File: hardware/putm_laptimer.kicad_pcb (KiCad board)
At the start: 4 copper layers, 92 x 63.5 mm, 48 parts, among them J1 Conn_01x22, J10 Conn_01x07, J11 Conn_01x07, J12 Conn_01x05, J13 Conn_01x05, J14 2091-1376, J2 Conn_01x22, J3 Conn_01x22, J4 Conn_01x22, J7 Conn_02x05_Odd_Even, J8 Conn_01x09, J9 M80-5001805

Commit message: Fixed borders
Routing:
- net +3V3: track 38.7 -> 35.7 mm, vias 10 -> 9
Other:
- outline, holes or cut-outs redrawn
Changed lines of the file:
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@@
 	(layers
 		(0 "F.Cu" signal "SIG1")
-		(4 "In1.Cu" power "GND1")
-		(6 "In2.Cu" power "GND2")
+		(4 "In1.Cu" power "GND")
+		(6 "In2.Cu" power "POWER")
 		(2 "B.Cu" signal "SIG2")
 		(13 "F.Paste" user)
@@
 	)
 	(gr_line
-		(start 195.5 58.5)
-		(end 144.5 58.5)
+		(start 195.1 58.5)
+		(end 144.9 58.5)
 		(stroke
 			(width 0.1)
@@
 	(gr_line
 		(start 204 52.5)
-		(end 195.5 52.5)
+		(end 195.9 52.5)
+		(stroke
+			(width 0.1)
+			(type default)
+		)
+		(layer "Edge.Cuts")
+	)
+	(gr_line
+		(start 144.5 58.1)
+		(end 144.5 52.9)
+		(stroke
+			(width 0.1)
+			(type default)
+		)
+		(layer "Edge.Cuts")
+	)
+	(gr_arc
+		(start 195.5 58.1)
+		(mid 195.382843 58.382843)
+		(end 195.1 58.5)
 		(stroke
 			(width 0.1)
@@
 	)
 	(gr_arc
+		(start 195.5 52.9)
+		(mid 195.617157 52.617157)
+		(end 195.9 52.5)
+		(stroke
+			(width 0.1)
+			(type default)
+		)
+		(layer "Edge.Cuts")
+	)
+	(gr_arc
 		(start 116.5 57)
 		(mid 117.818019 53.818019)
@@
 	)
 	(gr_line
-		(start 195.5 58.5)
-		(end 195.5 52.5)
+		(start 195.5 58.1)
+		(end 195.5 52.9)
+		(stroke
+			(width 0.1)
+			(type default)
+		)
+		(layer "Edge.Cuts")
+	)
+	(gr_arc
+		(start 144.1 52.5)
+		(mid 144.382843 52.617157)
+		(end 144.5 52.9)
 		(stroke
 			(width 0.1)
@@
 	)
 	(gr_arc
-		(start 208.5 111.5)
-		(mid 207.181981 114.681981)
-		(end 204 116)
+		(start 144.9 58.5)
+		(mid 144.617157 58.382843)
+		(end 144.5 58.1)
 		(stroke
 			(width 0.1)
@@
 		(layer "Edge.Cuts")
 	)
-	(gr_line
-		(start 121 52.5)
-		(end 144.5 52.5)
+	(gr_arc
+		(start 208.5 111.5)
+		(mid 207.181981 114.681981)
+		(end 204 116)
 		(stroke
 			(width 0.1)
@@
 	)
 	(gr_line
-		(start 144.5 52.5)
-		(end 144.5 58.5)
+		(start 121 52.5)
+		(end 144.1 52.5)
 		(stroke
 			(width 0.1)
@@
 	)
 	(gr_text "LCD"
-		(at 145.39 93.5 0)
+		(at 145.5 96 0)
 		(layer "F.SilkS")
 		(effects
@@
 	)
 	(segment
-		(start 197.6 83.17)
-		(end 195.83 83.17)
-		(width 0.4)
-		(layer "F.Cu")
-		(net 13)
-	)
-	(segment
 		(start 143.5 66.85)
 		(end 143.5 66)
@@
 	)
 	(segment
-		(start 195.83 83.17)
-		(end 195 84)
-		(width 0.4)
-		(layer "F.Cu")
-		(net 13)
-	)
-	(segment
 		(start 142 84.5)
 		(end 141.825 84.325)
@@
 		(net 13)
 	)
-	(via
-		(at 195 84)
-		(size 0.5)
-		(drill 0.3)
-		(layers "F.Cu" "B.Cu")
-		(net 13)
-	)

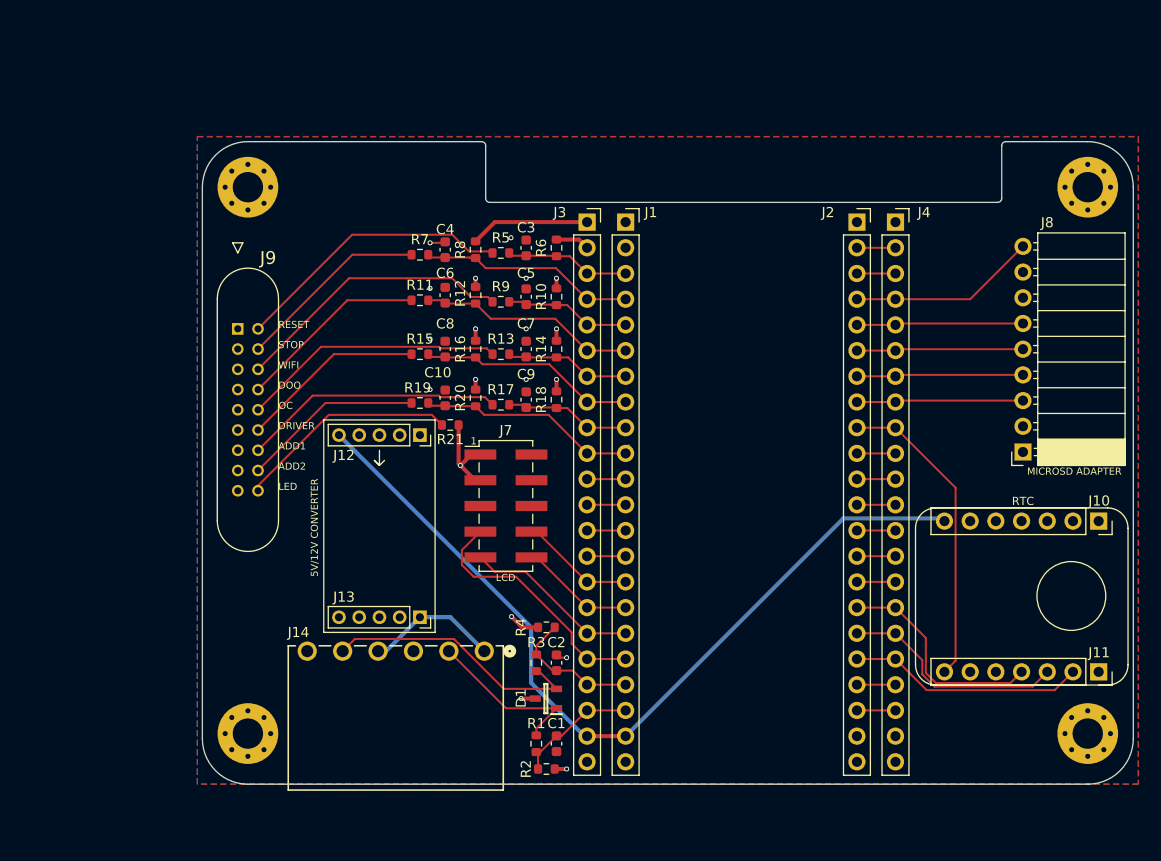
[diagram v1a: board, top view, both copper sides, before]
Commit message: Added modules info and links to connector schematics
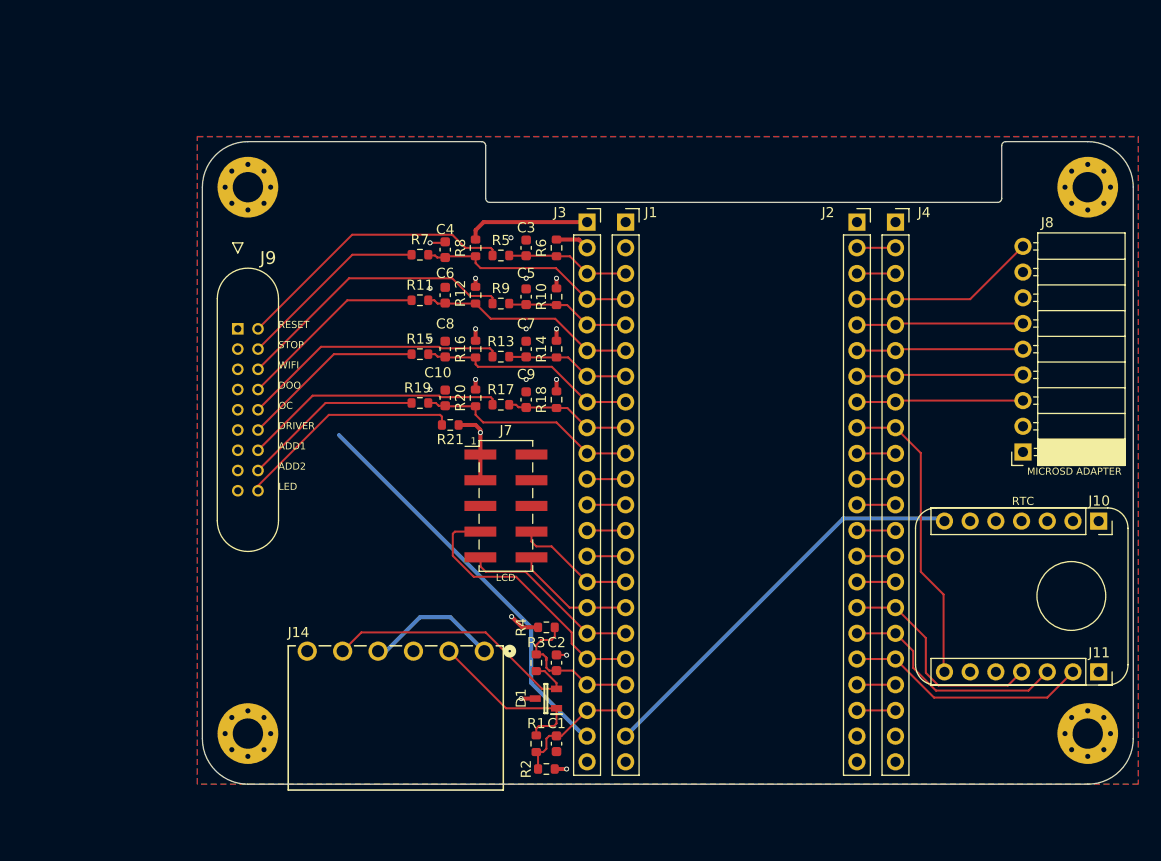
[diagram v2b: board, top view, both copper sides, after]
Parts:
- removed J12, J13: Conn_01x05, Connector_PinSocket_2.00mm:PinSocket_1x05_P2.00mm_Vertical
- moved R13 0.25 mm to (146.0, 73.8)
- moved R5 0.25 mm to (146.0, 63.8)
- moved R8 0.17 mm to (143.5, 63.0)
- moved R9 0.17 mm to (146.0, 68.5)
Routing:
- net +5V: track 84.8 -> 81.0 mm
- net /IO12_LCD_DC: track 24.7 -> 26.9 mm
- net /IO13_GATE2: track 13.7 -> 15.2 mm
- net /IO9_LCD_SPI_MOSI: track 11.4 -> 12.5 mm
- net +3V3: track 35.7 -> 34.6 mm
- net /IO39_RTC_NINT: track 30.9 -> 29.9 mm
- net Net-(D1-Pad2): track 26.9 -> 27.7 mm
- net Net-(D1-Pad1): track 16.5 -> 17.4 mm
- net /IO14_GATE1: track 13.5 -> 14.2 mm
- net /IO10_LCD_SPI_CS: track 11.4 -> 12.1 mm
- net /IO21_RTC_I2C_SCL: track 23.4 -> 24.0 mm
- net /IO11_LCD_SPI_CLK: track 17.9 -> 18.4 mm
- net /IO17_PIN: track 22.0 -> 22.5 mm
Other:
- board text removed: "5V/12V CONVERTER"

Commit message: Fixed routing
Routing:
- net +5V: track 81.0 -> 1.04 mm
- net +3V3: track 34.6 -> 61.7 mm, vias 9 -> 10
- net /ADD1_BTN: track 26.1 -> 28.7 mm, vias 0 -> 1
- net /OC_BTN: track 26.2 -> 28.3 mm, vias 0 -> 1
- net GND: track 3.95 -> 2.55 mm, vias 10 -> 5
- net /IO21_RTC_I2C_SCL: track 24.0 -> 25.3 mm
- net /PWR_LED: track 22.5 -> 21.4 mm, vias 0 -> 1
- net /IO47_RTC_I2C_SDA: track 22.9 -> 23.5 mm
- net /WIFI_BTN: track 28.1 -> 28.7 mm, vias 0 -> 1
- net /RST_BTN: track 28.0 -> 27.7 mm, vias 0 -> 1
- net /DOO_BTN: track 18.8 -> 19.0 mm, vias 0 -> 1
- net /STOP_BTN: vias 0 -> 1
- net /DRIVER_BTN: vias 0 -> 1
- net /ADD2_BTN: vias 0 -> 1
- added copper zone on In2.Cu, net +12V
- added copper zone on In2.Cu, net +5V

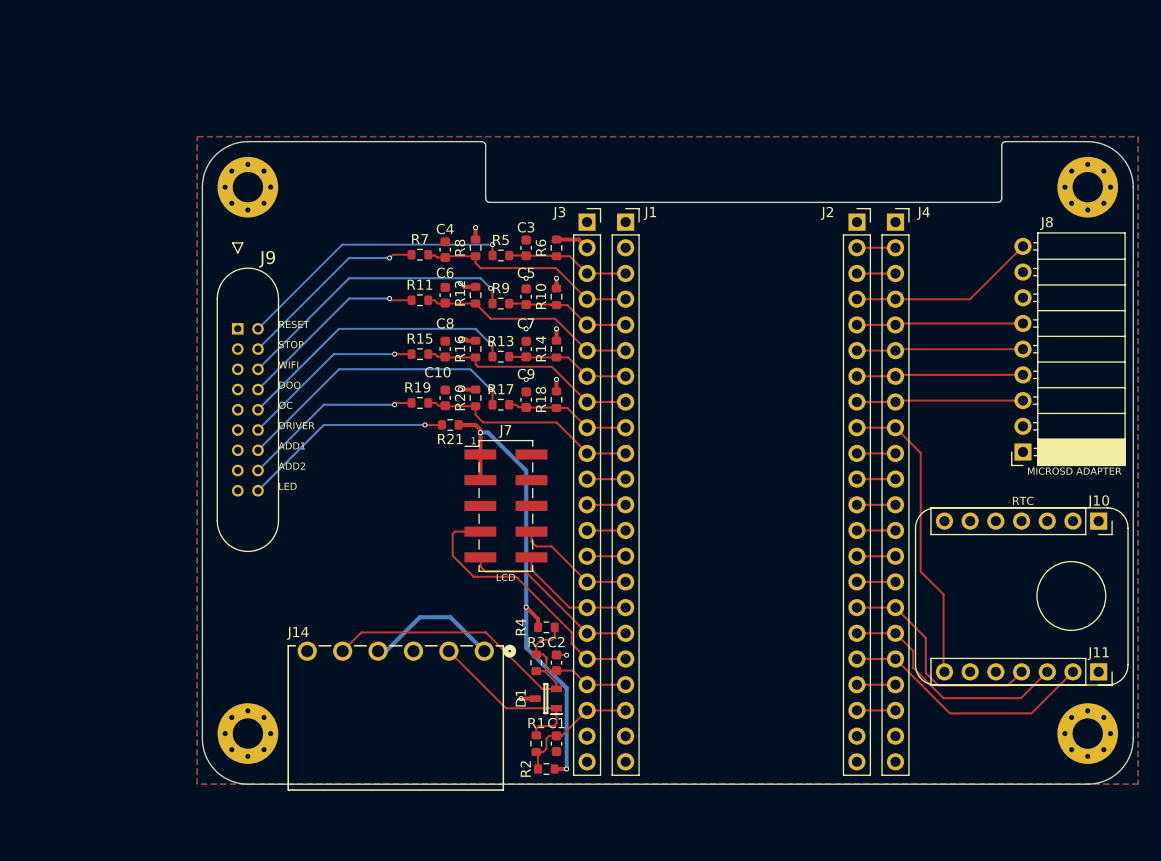
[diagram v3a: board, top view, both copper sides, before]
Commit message: Changed layout, changed gate connector, added 12V battery connector and buck converter pins
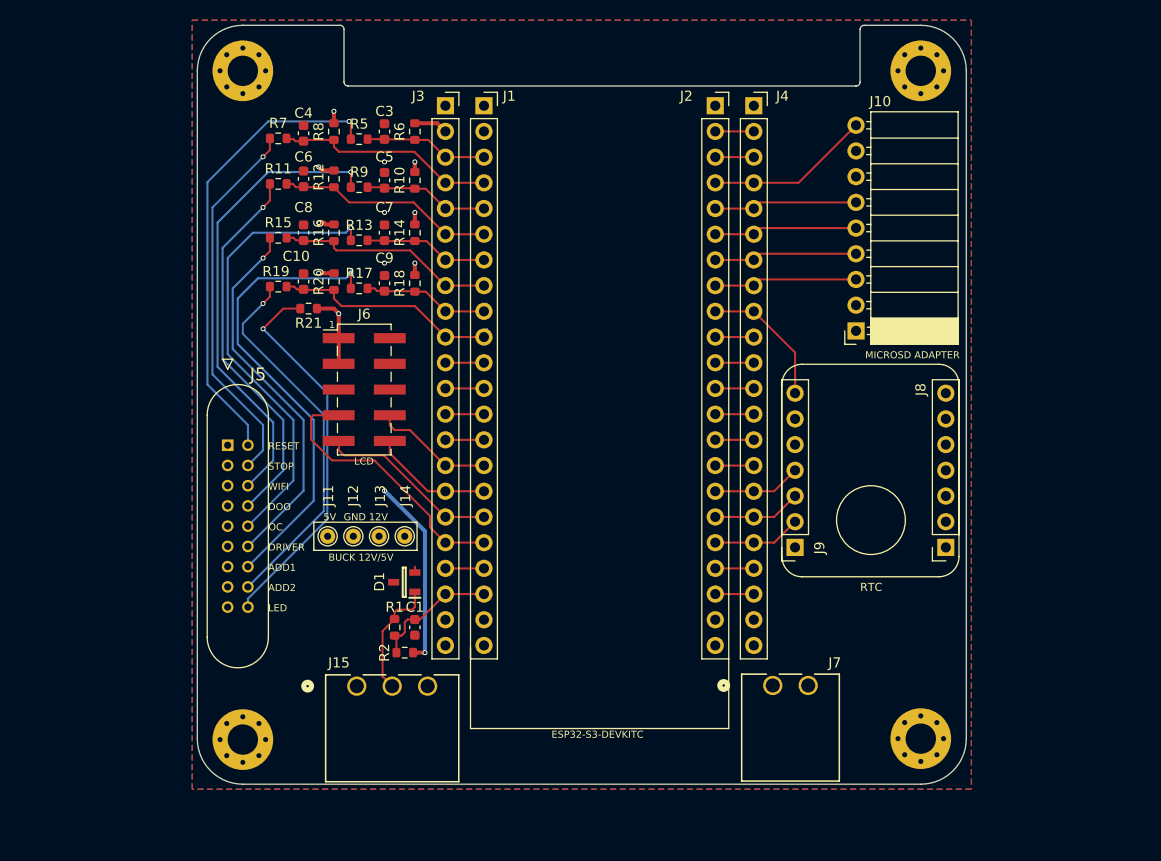
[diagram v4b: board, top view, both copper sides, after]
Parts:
- removed C2: 100n, Capacitor_SMD:C_0603_1608Metric
- removed R3: 1k, Resistor_SMD:R_0603_1608Metric
- removed R4: 10k, Resistor_SMD:R_0603_1608Metric
- added J11: Conn_01x01, TestPoint:TestPoint_THTPad_D1.5mm_Drill0.7mm, F.Cu at (128.9, 91.5)
- added J12: Conn_01x01, TestPoint:TestPoint_THTPad_D1.5mm_Drill0.7mm, F.Cu at (131.4, 91.5)
- added J13: Conn_01x01, TestPoint:TestPoint_THTPad_D1.5mm_Drill0.7mm, F.Cu at (134.0, 91.5)
- added J15: 734-163, Footprint:CONN3_734-163_WAG, F.Cu at (131.8, 106.3)
- added J7: 734-162, Footprint:CONN2_734-162_WAG, F.Cu at (172.9, 106.2)
- J14: value 2091-1376 -> Conn_01x01; footprint Footprint:CONN6_2091-1376_WAG -> TestPoint:TestPoint_THTPad_D1.5mm_Drill0.7mm
- moved J9 32.4 mm to (175.1, 92.6), turned to 180 degrees
- moved J10 20.4 mm to (181.1, 71.2)
- moved REF** 20.1 mm to (187.5, 45.5)
- moved C1 18.1 mm to (137.5, 100.5)
- moved C10 18.1 mm to (126.5, 66.3)
- moved C3 18.1 mm to (134.5, 51.5)
- moved C4 18.1 mm to (126.5, 51.7)
- moved C5 18.1 mm to (134.5, 56.3)
- moved C6 18.1 mm to (126.5, 56.2)
- moved C7 18.1 mm to (134.5, 61.5)
- moved C8 18.1 mm to (126.5, 61.5)
- moved C9 18.1 mm to (134.5, 66.5)
- moved D1 18.1 mm to (136.4, 96.0)
- moved J1 18.1 mm to (144.3, 49.0)
- moved J2 18.1 mm to (167.2, 49.0)
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- renumbered J8 to J10, J9 to J5, J7 to J6, J10 to J8, J11 to J9
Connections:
- D1 pad 2: Net-(D1-Pad2) -> GND
- J14 pad 1: +12V -> +5V
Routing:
- net Net-(D1-Pad2): track 27.7 -> 0.00 mm
- net +3V3: track 61.7 -> 39.7 mm
- net /ADD2_BTN: track 17.9 -> 37.2 mm
- net /DRIVER_BTN: track 18.3 -> 37.2 mm
- net /DOO_BTN: track 19.0 -> 37.7 mm
- net /STOP_BTN: track 19.0 -> 37.4 mm
- net /RST_BTN: track 27.7 -> 46.0 mm
- net /ADD1_BTN: track 28.7 -> 46.3 mm
- net /OC_BTN: track 28.3 -> 45.7 mm
- net /WIFI_BTN: track 28.7 -> 46.1 mm
- net /IO21_RTC_I2C_SCL: track 25.3 -> 8.74 mm
- net /PWR_LED: track 21.4 -> 37.9 mm
- net /IO39_RTC_NINT: track 29.9 -> 13.6 mm
- net /IO47_RTC_I2C_SDA: track 23.5 -> 8.74 mm
- net /IO48_RTC_CLKOUT: track 22.0 -> 8.74 mm
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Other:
- board size 92 x 63.5 mm -> 76 x 75 mm
- board text added: "12V"
- board text added: "5V"
- board text added: "BUCK 12V/5V"
- board text added: "ESP32-S3-DEVKITC"
- board text added: "GND"

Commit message: Fixed schematics
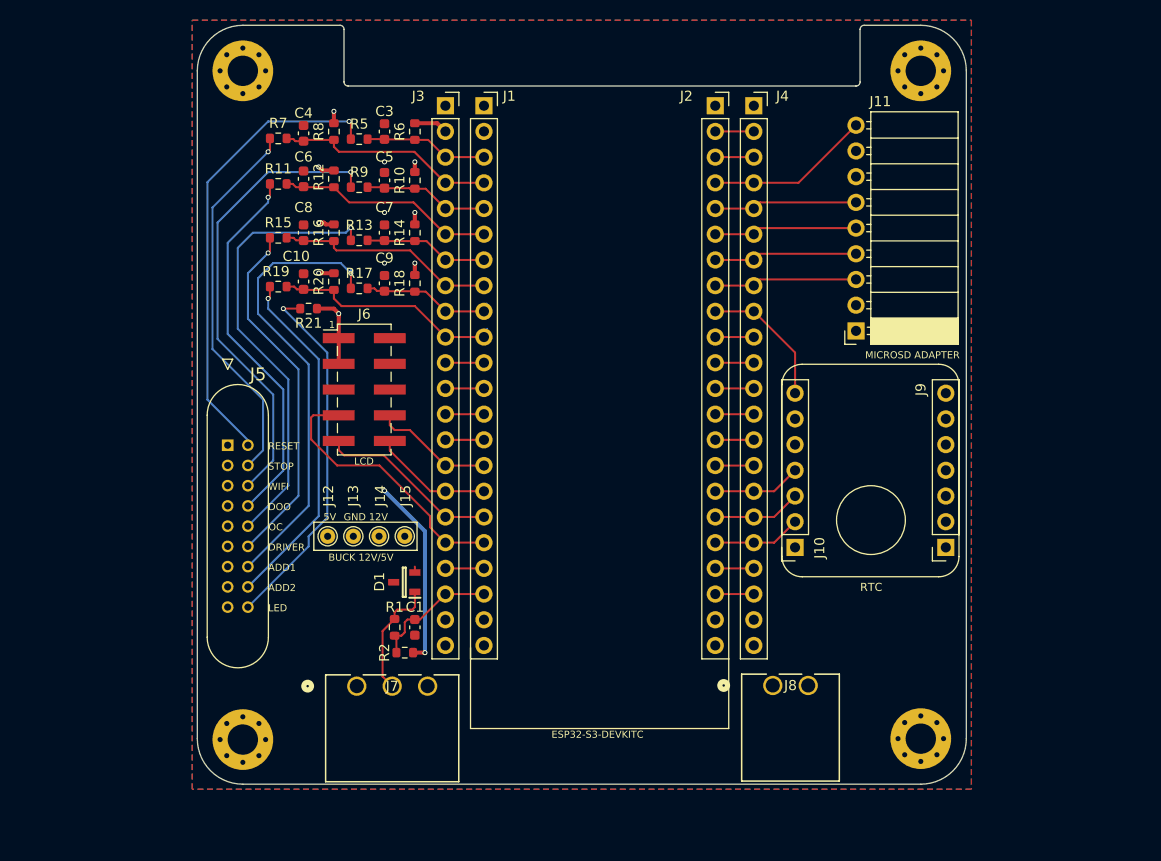
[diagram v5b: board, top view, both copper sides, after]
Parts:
- renumbered J9 to J10, J10 to J11, J11 to J12, J12 to J13, J13 to J14, J14 to J15, J15 to J7, J7 to J8, J8 to J9
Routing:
- net /ADD2_BTN: track 37.2 -> 34.7 mm
- net /PWR_LED: track 37.9 -> 36.2 mm
- net /DRIVER_BTN: track 37.2 -> 35.5 mm
- net /OC_BTN: track 45.7 -> 44.5 mm
- net /ADD1_BTN: track 46.3 -> 45.1 mm

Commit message: Fixed pcb layout
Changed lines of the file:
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@@
 	)
 	(segment
-		(start 131.175 55.5)
+		(start 131.175 55.675)
 		(end 131.175 57)
 		(width 0.2)
@@
 		(net 32)
 	)
+	(segment
+		(start 131 55.5)
+		(end 131.175 55.675)
+		(width 0.2)
+		(layer "F.Cu")
+		(net 32)
+	)
 	(via
-		(at 131.175 55.5)
+		(at 131 55.5)
 		(size 0.5)
 		(drill 0.3)
 		(layers "F.Cu" "B.Cu")
-		(net 32)
-	)
-	(segment
-		(start 123.005 55.505)
-		(end 123 55.5)
-		(width 0.2)
-		(layer "B.Cu")
-		(net 32)
-	)
-	(segment
-		(start 123 55.5)
-		(end 118 60.5)
-		(width 0.2)
-		(layer "B.Cu")
-		(net 32)
-	)
-	(segment
-		(start 131.17 55.505)
-		(end 123.005 55.505)
-		(width 0.2)
-		(layer "B.Cu")
-		(net 32)
-	)
-	(segment
-		(start 123.5 84)
-		(end 121 86.5)
-		(width 0.2)
-		(layer "B.Cu")
 		(net 32)
 	)
@@
 	)
 	(segment
-		(start 131.175 55.5)
-		(end 131.17 55.505)
+		(start 123 55.5)
+		(end 118 60.5)
 		(width 0.2)
 		(layer "B.Cu")
@@
 		(width 0.2)
 		(layer "B.Cu")
+		(net 32)
+	)
+	(segment
+		(start 130.995 55.505)
+		(end 123.005 55.505)
+		(width 0.2)
+		(layer "B.Cu")
+		(net 32)
+	)
+	(segment
+		(start 123.005 55.505)
+		(end 123 55.5)
+		(width 0.2)
+		(layer "B.Cu")
+		(net 32)
+	)
+	(segment
+		(start 131 55.5)
+		(end 130.995 55.505)
+		(width 0.2)
+		(layer "B.Cu")
+		(net 32)
+	)
+	(segment
+		(start 123.5 84)
+		(end 121 86.5)
+		(width 0.2)
+		(layer "B.Cu")
